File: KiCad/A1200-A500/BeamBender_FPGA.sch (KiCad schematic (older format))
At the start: 20 parts, among them J6 Conn_02x06_Odd_Even, U2 GW1NR-UV9LQ144P, U5 AK5720VT, X3 5.0x3.2mm

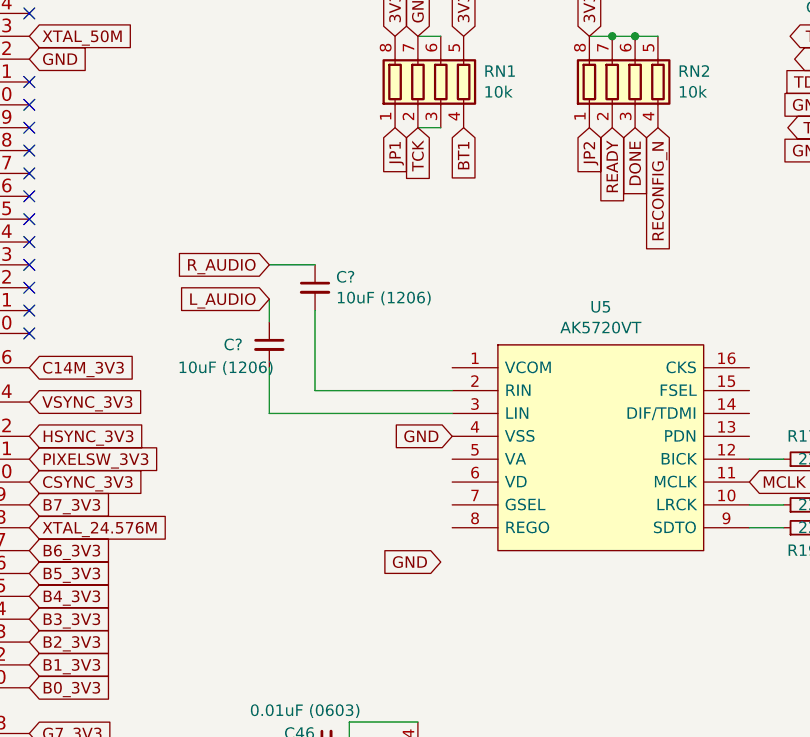
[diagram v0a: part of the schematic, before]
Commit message: Added a 0.47uF cap for ADC-chip VCOM pin (Voltage Reference)
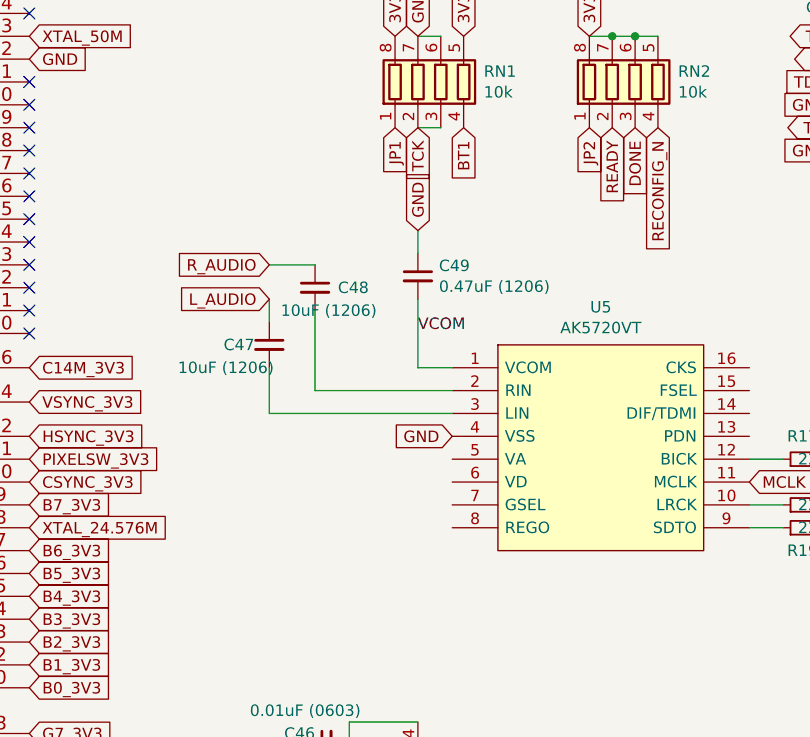
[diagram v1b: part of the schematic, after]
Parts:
- added C49: 0.47uF (1206), Capacitor_SMD:C_1206_3216Metric_Pad1.33x1.80mm_HandSolder, symbol Device:C_Small
- gave numbers to parts that had none: 2
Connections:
- net GND: now also C49.1
- net VCOM: now reaches U5.1 (VCOM)
- net VCOM: now also C49.2
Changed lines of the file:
@@
 	1    0    0    -1
 $EndComp
-Text GLabel 8300 4100 0    50   Input ~ 0
+Text GLabel 8200 2650 1    50   Input ~ 0
 GND
 Text GLabel 8350 3550 0    50   Input ~ 0
@@
 R_AUDIO
 $Comp
-L Device:C_Small C?
+L Device:C_Small C48
 U 1 1 667B6179
 P 7750 2900
-F 0 "C?" H 7842 2946 50  0000 L CNN
-F 1 "10uF (1206)" H 7842 2855 50  0000 L CNN
+F 0 "C48" H 7850 2900 50  0000 L CNN
+F 1 "10uF (1206)" H 7600 2800 50  0000 L CNN
 F 2 "Capacitor_SMD:C_1206_3216Metric_Pad1.33x1.80mm_HandSolder" H 7750 2900 50  0001 C CNN
 F 3 "~" H 7750 2900 50  0001 C CNN
@@
 $EndComp
 $Comp
-L Device:C_Small C?
+L Device:C_Small C47
 U 1 1 667B7F1E
 P 7550 3150
-F 0 "C?" H 7350 3150 50  0000 L CNN
+F 0 "C47" H 7350 3150 50  0000 L CNN
 F 1 "10uF (1206)" H 7150 3050 50  0000 L CNN
 F 2 "Capacitor_SMD:C_1206_3216Metric_Pad1.33x1.80mm_HandSolder" H 7550 3150 50  0001 C CNN
@@
 Wire Wire Line
 	7550 2950 7550 3050
+$Comp
+L Device:C_Small C49
+U 1 1 667DACF3
+P 8200 2850
+F 0 "C49" H 8292 2896 50  0000 L CNN
+F 1 "0.47uF (1206)" H 8292 2805 50  0000 L CNN
+F 2 "Capacitor_SMD:C_1206_3216Metric_Pad1.33x1.80mm_HandSolder" H 8200 2850 50  0001 C CNN
+F 3 "~" H 8200 2850 50  0001 C CNN
+	1    8200 2850
+	1    0    0    -1
+$EndComp
+Wire Wire Line
+	8200 2950 8200 3250
+Wire Wire Line
+	8200 3250 8350 3250
+Text Label 8200 3100 0    50   ~ 0
+VCOM
+Wire Wire Line
+	8200 2650 8200 2750
 $EndSCHEMATC

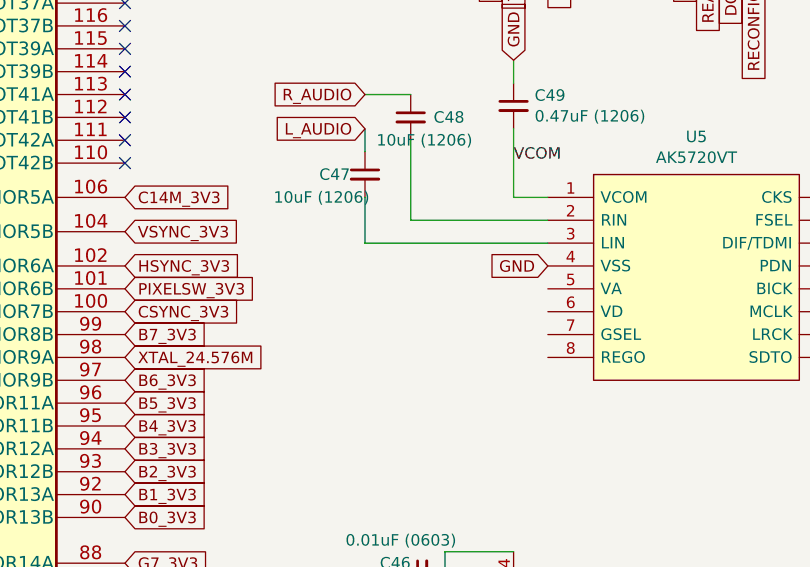
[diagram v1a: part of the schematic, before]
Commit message: Repositioning of the AK5720 chip and routed the analog supply with 5V and digital supply with 3V3
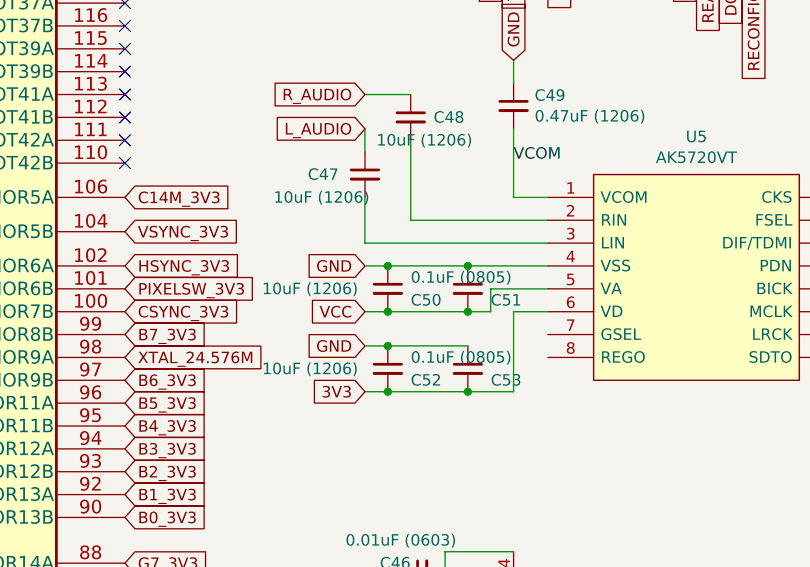
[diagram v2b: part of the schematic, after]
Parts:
- added C50, C52: 10uF (1206), Capacitor_SMD:C_1206_3216Metric_Pad1.33x1.80mm_HandSolder, symbol Device:C_Small
- added C51, C53: 0.1uF (0805), Capacitor_SMD:C_0805_2012Metric_Pad1.18x1.45mm_HandSolder, symbol Device:C_Small
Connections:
- net 3V3: now also U5.6 (VD), C52.2, C53.2
- net GND: now also C50.1, C51.1, C52.1, C53.1
- net VCC: now reaches U5.5 (VA)
- net VCC: now also C50.2, C51.2
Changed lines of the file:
@@
 Text GLabel 8200 2650 1    50   Input ~ 0
-GND
-Text GLabel 8350 3550 0    50   Input ~ 0
 GND
 Text GLabel 10100 3950 2    50   Output ~ 0
@@
 U 1 1 667B7F1E
 P 7550 3150
-F 0 "C47" H 7350 3150 50  0000 L CNN
+F 0 "C47" H 7300 3150 50  0000 L CNN
 F 1 "10uF (1206)" H 7150 3050 50  0000 L CNN
 F 2 "Capacitor_SMD:C_1206_3216Metric_Pad1.33x1.80mm_HandSolder" H 7550 3150 50  0001 C CNN
@@
 Wire Wire Line
 	8200 2650 8200 2750
+Text GLabel 7550 3750 0    50   Input ~ 0
+VCC
+Text GLabel 7550 3550 0    50   Input ~ 0
+GND
+Connection ~ 7650 3550
+Wire Wire Line
+	7550 3550 7650 3550
+Wire Wire Line
+	7650 3550 8000 3550
+$Comp
+L Device:C_Small C50
+U 1 1 66802342
+P 7650 3650
+F 0 "C50" H 7750 3600 50  0000 L CNN
+F 1 "10uF (1206)" H 7100 3650 50  0000 L CNN
+F 2 "Capacitor_SMD:C_1206_3216Metric_Pad1.33x1.80mm_HandSolder" H 7650 3650 50  0001 C CNN
+F 3 "~" H 7650 3650 50  0001 C CNN
+	1    7650 3650
+	1    0    0    -1
+$EndComp
+$Comp
+L Device:C_Small C?
+U 1 1 66811715
+P 8000 3650
+AR Path="/66811715" Ref="C?"  Part="1"
+AR Path="/6541C824/66811715" Ref="C51"  Part="1"
+F 0 "C51" H 8100 3600 50  0000 L CNN
+F 1 "0.1uF (0805)" H 7750 3700 50  0000 L CNN
+F 2 "Capacitor_SMD:C_0805_2012Metric_Pad1.18x1.45mm_HandSolder" H 8000 3650 50  0001 C CNN
+F 3 "~" H 8000 3650 50  0001 C CNN
+	1    8000 3650
+	1    0    0    -1
+$EndComp
+Connection ~ 8000 3550
+Wire Wire Line
+	8000 3550 8350 3550
+Wire Wire Line
+	8000 3750 7650 3750
+Wire Wire Line
+	7550 3750 7650 3750
+Connection ~ 7650 3750
+Text GLabel 7550 3900 0    50   Input ~ 0
+GND
+Connection ~ 7650 3900
+Wire Wire Line
+	7550 3900 7650 3900
+Wire Wire Line
+	7650 3900 8000 3900
+$Comp
+L Device:C_Small C52
+U 1 1 668486F6
+P 7650 4000
+F 0 "C52" H 7750 3950 50  0000 L CNN
+F 1 "10uF (1206)" H 7100 4000 50  0000 L CNN
+F 2 "Capacitor_SMD:C_1206_3216Metric_Pad1.33x1.80mm_HandSolder" H 7650 4000 50  0001 C CNN
+F 3 "~" H 7650 4000 50  0001 C CNN
+	1    7650 4000
+	1    0    0    -1
+$EndComp
+$Comp
+L Device:C_Small C?
+U 1 1 66848700
+P 8000 4000
+AR Path="/66848700" Ref="C?"  Part="1"
+AR Path="/6541C824/66848700" Ref="C53"  Part="1"
+F 0 "C53" H 8100 3950 50  0000 L CNN
+F 1 "0.1uF (0805)" H 7750 4050 50  0000 L CNN
+F 2 "Capacitor_SMD:C_0805_2012Metric_Pad1.18x1.45mm_HandSolder" H 8000 4000 50  0001 C CNN
+F 3 "~" H 8000 4000 50  0001 C CNN
+	1    8000 4000
+	1    0    0    -1
+$EndComp
+Wire Wire Line
+	8200 4100 8000 4100
+Wire Wire Line
+	8000 4100 7650 4100
+Connection ~ 8000 4100
+Wire Wire Line
+	7550 4100 7650 4100
+Connection ~ 7650 4100
+Text GLabel 7550 4100 0    50   Input ~ 0
+3V3
+Wire Wire Line
+	8200 4100 8200 3750
+Wire Wire Line
+	8200 3750 8350 3750
+Wire Wire Line
+	8100 3650 8100 3750
+Wire Wire Line
+	8100 3750 8000 3750
+Wire Wire Line
+	8100 3650 8350 3650
+Connection ~ 8000 3750
 $EndSCHEMATC

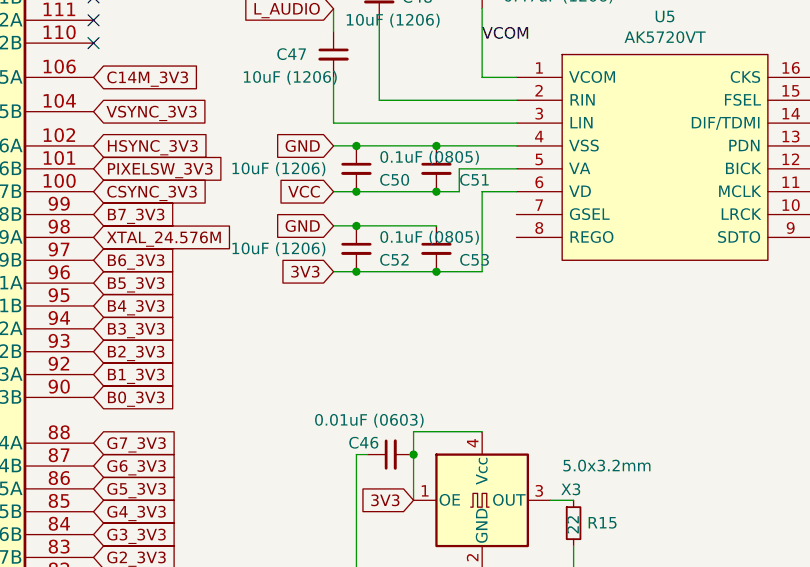
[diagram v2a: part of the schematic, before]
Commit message: Added a pull-up resistor for GSEL (Gain-Select) input pin with a solder JP to be able to turn gain off = GND
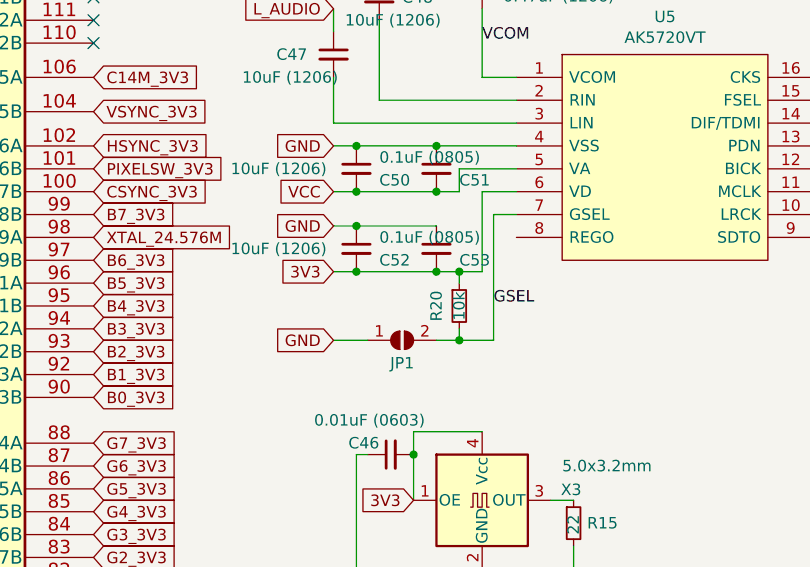
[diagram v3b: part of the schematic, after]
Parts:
- added JP1: SolderJumper_2_Open, Jumper:SolderJumper-2_P1.3mm_Open_Pad1.0x1.5mm, symbol Jumper:SolderJumper_2_Open
- added R20: 10k, Resistor_SMD:R_0805_2012Metric_Pad1.20x1.40mm_HandSolder, symbol Device:R_Small
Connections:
- net 3V3: now also R20.1
- net GND: now also JP1.1 (A)
- net GSEL: now reaches U5.7 (GSEL)
- net GSEL: now also JP1.2 (B), R20.2
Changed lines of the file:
@@
 $EndComp
 Wire Wire Line
-	8200 4100 8000 4100
+	8200 4100 8100 4100
 Wire Wire Line
 	8000 4100 7650 4100
@@
 3V3
 Wire Wire Line
-	8200 4100 8200 3750
-Wire Wire Line
 	8200 3750 8350 3750
 Wire Wire Line
@@
 	8100 3650 8350 3650
 Connection ~ 8000 3750
+Wire Wire Line
+	8200 3750 8200 4100
+Wire Wire Line
+	8350 3850 8250 3850
+$Comp
+L Jumper:SolderJumper_2_Open JP1
+U 1 1 668D7347
+P 7850 4400
+F 0 "JP1" H 7850 4300 50  0000 C CNN
+F 1 "SolderJumper_2_Open" H 7850 4514 50  0001 C CNN
+F 2 "Jumper:SolderJumper-2_P1.3mm_Open_Pad1.0x1.5mm" H 7850 4400 50  0001 C CNN
+F 3 "~" H 7850 4400 50  0001 C CNN
+	1    7850 4400
+	1    0    0    -1
+$EndComp
+$Comp
+L Device:R_Small R20
+U 1 1 668DB86F
+P 8100 4250
+F 0 "R20" V 8000 4250 50  0000 C CNN
+F 1 "10k" V 8100 4250 50  0000 C CNN
+F 2 "Resistor_SMD:R_0805_2012Metric_Pad1.20x1.40mm_HandSolder" H 8100 4250 50  0001 C CNN
+F 3 "~" H 8100 4250 50  0001 C CNN
+	1    8100 4250
+	1    0    0    -1
+$EndComp
+Wire Wire Line
+	8000 4400 8100 4400
+Wire Wire Line
+	8250 3850 8250 4400
+Text GLabel 7550 4400 0    50   Input ~ 0
+GND
+Wire Wire Line
+	7550 4400 7700 4400
+Wire Wire Line
+	8100 4100 8100 4150
+Connection ~ 8100 4100
+Wire Wire Line
+	8100 4100 8000 4100
+Wire Wire Line
+	8100 4350 8100 4400
+Connection ~ 8100 4400
+Wire Wire Line
+	8100 4400 8250 4400
+Text Label 8250 4250 0    50   ~ 0
+GSEL
 $EndSCHEMATC
